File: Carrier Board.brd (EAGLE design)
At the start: 90 x 38.6 mm, 55 parts, among them J1 H4P-SMD-2.0, J2 H4P-SMD-2.0, J4 S2B-PH-SM4-TB(LF)(SN), J5 S2B-PH-SM4-TB(LF)(SN), Q1 MMBT2222A, SW2 MF-SW-TACT-6MM, U1 TMP36GRTZ, U2 TPL5010, U3 MB85RC64, U7 NAND

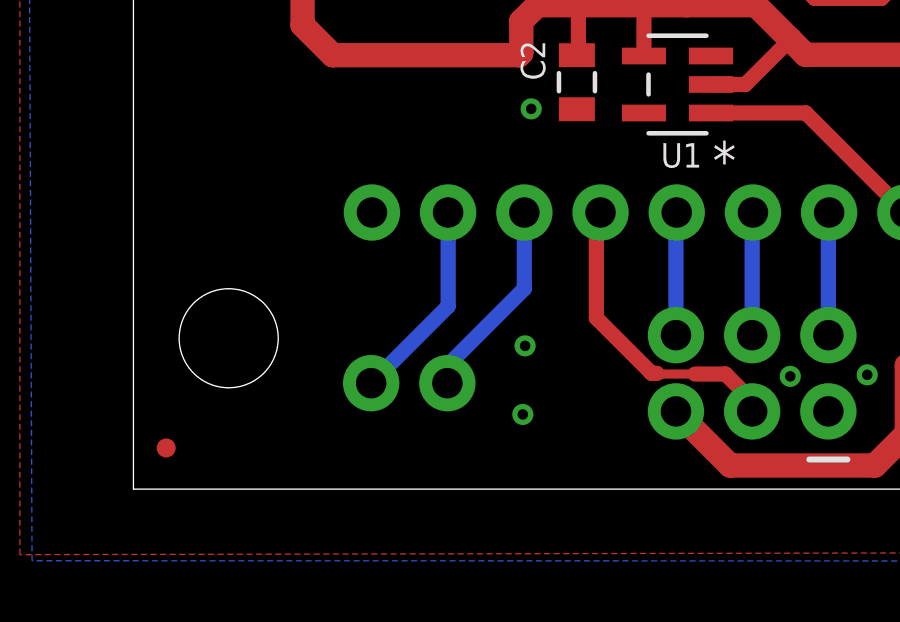
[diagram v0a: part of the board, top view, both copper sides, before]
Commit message: v1.1 - Added a GND pin to serial
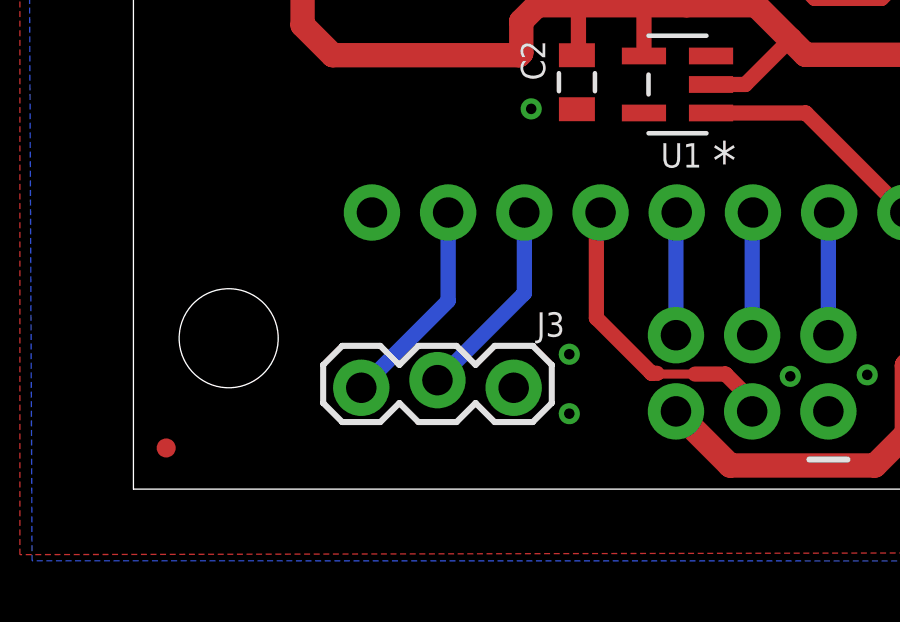
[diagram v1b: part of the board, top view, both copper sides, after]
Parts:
- J3: device SparkFun-Connectors:1X02 -> SparkFun-Connectors:1X03_LOCK
- moved J3 2.21 mm to (12.7, 3.51), flipped to the top, turned to 180 degrees
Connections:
- net GND: now also J3.1
- net RX: now also J3.2; no longer J3.1
- net TX: now also J3.3; no longer J3.2
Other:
- board text added: "GND Rx Tx"
- board text removed: "Rx Tx"

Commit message: Fixed Analoge Header Pins
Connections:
- net A0: now also J1.1; no longer J1.3
- net A1: now also J1.2; no longer J1.4
- net GND: now also J1.4; no longer J1.1
- net VCC-EXT: now also J1.3; no longer J1.2
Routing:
- net A0: track 12.8 -> 5.08 mm
- net A1: track 18.1 -> 13.0 mm
- net USER-SW: track 36.3 -> 39.1 mm
- net VCC-EXT: track 34.6 -> 36.0 mm, vias 1 -> 2
- net VCC2-EXT: vias 1 -> 2
- net SDA: vias 1 -> 2
- net SCL: vias 1 -> 2

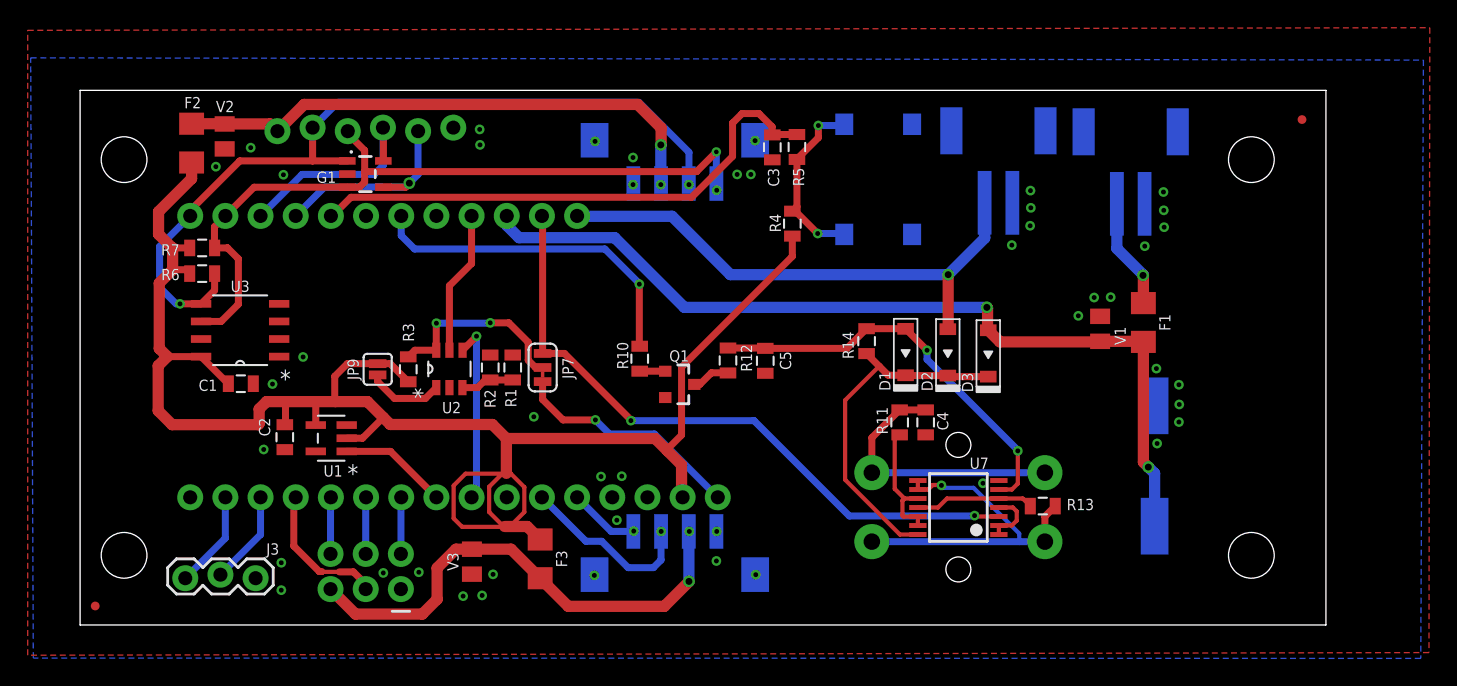
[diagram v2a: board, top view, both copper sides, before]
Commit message: Next major revision - Added RTC
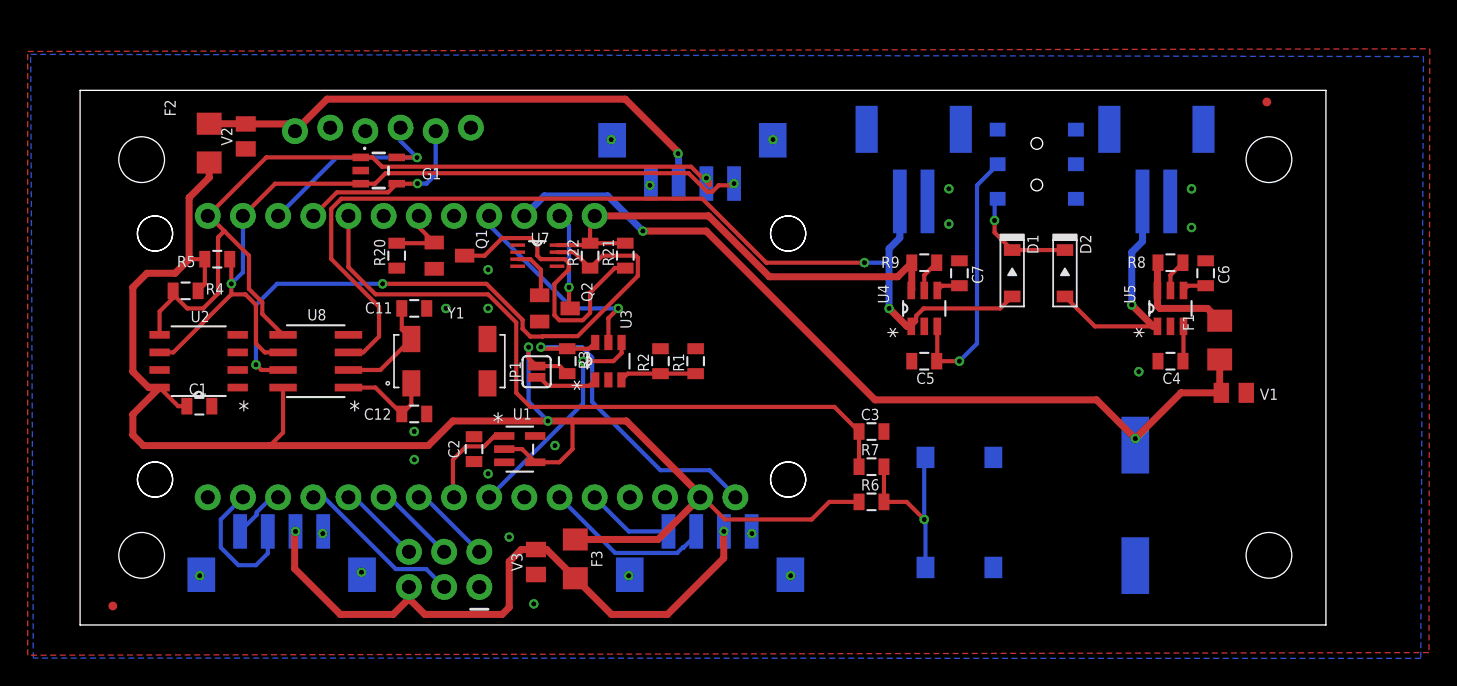
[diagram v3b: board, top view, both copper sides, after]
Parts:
- removed BORON/ARGON/XENON: PARTICLE-DEVICES-BORON, Carrier Board:PARTICLE-DEVICES_BORON
- removed D3: MF-DIO-SOD123-BAT42, MF_Discrete_Semiconductor:SOD-123
- removed JP7: JUMPER-SMT_3_1-NC_TRACE_SILK, SparkFun-Jumpers:SMT-JUMPER_3_1-NC_TRACE_SILK
- removed JP9: JUMPER-SMT_2_NC_PASTE_SILK, SparkFun-Jumpers:SMT-JUMPER_2_NC_PASTE_SILK
- removed R10: 10k, SparkFun-Passives:0805
- removed R11, R13, R14: 100k, SparkFun-Passives:0805
- removed R12: 100, SparkFun-Passives:0805
- removed S2: B3F-4000, adafruit:B3F-40XX-ROUND
- removed SW2: MF-SW-TACT-6MM, MF_Switches:TACT6MM
- added C11: 10pF, SparkFun-Capacitors:0805@1
- added C12: 8.2pF, SparkFun-Capacitors:0805@1
- added C6, C7: 0.1uF, SparkFun-Capacitors:0805@1
- added H1, H2, H3, H4: STAND-OFF-M2.5, Custom Components:STAND-OFF-M2.5
- added JP2: (no value), SparkFun-Connectors:1X06_LOCK
- added P1: PARTICLE-DEVICES-BORON, Carrier Board:PARTICLE-DEVICES_BORON
- added Q2: BSS138, transistor-small-signal:SOT23
- added R20, R21, R22: 10k, SparkFun-Passives:0805
- added R8, R9: 100, SparkFun-Passives:0805
- added S1: (no value), SparkFun-Switches:SWITCH_DPDT_SMD_AYZ0202
- added SW1: MF-SW-TACT-6MM, MF_Switches:TACT6MM
- added U4, U5: TPS22810, Custom Components:SOT-23-6
- added U8: MCP79410T-I/SN, Custom Components:SOIC8-N_MC
- added Y1: ECS-.327-6-17X-TR, Custom Components:XTAL_ECS-.327-6-17X-TR
- C4: value 0.1uF -> 10nF
- C5: value 1uF -> 10nF
- D1, D2: value MF-DIO-SOD123-BAT42 -> BAT42
- F1: value 1.5A - SLOW BLOW -> 6V/0.5A
- F2, F3: value 500mA - FAST BLOW -> 6V/0.5A
- J3: value (none) -> H4P-SMD-2.0; device SparkFun-Connectors:1X03_LOCK -> OPL_Connector:HW4-SMD-2.0
- J4: value S2B-PH-SM4-TB(LF)(SN) -> (none); device SparkFun-Connectors:JST-2-SMD -> SparkFun-Connectors:2X3
- J6: value (none) -> S2B-PH-SM4-TB(LF)(SN); device SparkFun-Connectors:2X3 -> SparkFun-Connectors:JST-2-SMD
- JP1: value (none) -> JUMPER-SMT_2_NC_PASTE_SILK; device SparkFun-Connectors:1X06_LOCK -> SparkFun-Jumpers:SMT-JUMPER_2_NC_PASTE_SILK
- JP3, JP4, JP5, JP6: device SparkFun:STAND-OFF -> SparkFun-Hardware:STAND-OFF
- Q1: value MMBT2222A -> BSS138; device SparkFun-DiscreteSemi:SOT23-3 -> transistor-small-signal:SOT23
- R4: value 100k -> 4.7k
- R5: value 10k -> 4.7k
- R6: value 4.7k -> 100k
- R7: value 4.7k -> 10k
- U2: value TPL5010 -> MB85RC64; device Custom Components:TSOT-23 -> Fujitsu_By_element14_Batch_1:SOIC127P600X175-8N
- U3: value MB85RC64 -> TPL5010; device Fujitsu_By_element14_Batch_1:SOIC127P600X175-8N -> Custom Components:TSOT-23
- U7: value NAND -> NL17SZ74USG; device adafruit:MC14093B-TSSOP14 -> Custom Components:SOP50P310X90-8N
- moved FRAME3 102.4 mm to (90.4, 19.3)
- moved J6 63.1 mm to (77.7, 34.3)
- moved J4 56.5 mm to (28.8, 2.74)
- moved R6 51.1 mm to (57.1, 8.89)
- moved R7 50.9 mm to (57.1, 11.4), turned to 0 degrees
- moved R4 44.1 mm to (7.62, 24.1), turned to 0 degrees
- moved R5 42.6 mm to (9.91, 26.4), turned to 180 degrees
- moved U7 35.4 mm to (33.0, 26.7), turned to 0 degrees
- moved U3 26.7 mm to (38.2, 19.1), turned to 90 degrees
- moved C3 21.7 mm to (57.1, 14.0), turned to 0 degrees
- moved Q1 19.0 mm to (26.7, 26.7)
- moved JP1 18.6 mm to (33.0, 18.3), flipped to the top, turned to 90 degrees
- moved C4 18.2 mm to (78.7, 19.1), turned to 180 degrees
- moved U2 18.1 mm to (8.56, 19.1), turned to 180 degrees
- moved C2 13.7 mm to (28.4, 12.7), turned to 90 degrees
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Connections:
- removed net !HARD-RESET: C5.1, D1.ANODE, R12.1, R14.1, U7.6
- removed net BUTTON-STATE: R13.1, U7.11, U7.5
- removed net DC-IN-EXT: F1.1, J4.2
- removed net ENABLE-PWR: D1.CATHODE, D2.CATHODE, D3.CATHODE, R14.2, U7.14
- removed net HARD-RESET: BORON/ARGON/XENON.D6, R10.2
- removed net N$1: U7.1, U7.2, U7.4
- removed net N$19: Q1.3, R12.2
- removed net N$24: C4.1, R11.2, S2.3, S2.4
- removed net N$25: R13.2, S2.1, S2.2, U7.8, U7.9
- removed net RESET: JP7.2, R3.1, U2.6
- new net BATT-IN: D1.ANODE, J5.2, U4.1, U8.3
- new net DEEP-SLEEP: P1.D6, Q1.1, R20.2
- new net EN/UVLO: C4.1, C5.1, S1.2, U4.3, U5.3
- new net N$10: C7.1, U4.4
- new net N$11: D2.ANODE, J6.2, U5.1
- new net N$12: R9.1, U4.5
- new net N$13: Q2.1, U7.3
- new net N$15: C12.1, U8.1, Y1.1
- new net N$2: P1.D5
- new net N$5: C6.1, U5.4
- new net N$6: R8.1, U5.5
- new net N$7: F1.1, R8.2, U5.6
- new net N$9: D1.CATHODE, D2.CATHODE, S1.3
- new net RTC-INT: R22.1, U7.7, U8.7
- net !RST: now also P1.RST, R3.1, U3.6; no longer BORON/ARGON/XENON.RST, JP7.3
- net A0: now also P1.A0; no longer BORON/ARGON/XENON.A0
- net A1: now also P1.A1; no longer BORON/ARGON/XENON.A1
- net A2: now also P1.A2; no longer BORON/ARGON/XENON.A2
- net D2: now also JP2.3, P1.D2; no longer BORON/ARGON/XENON.D2, JP1.3
- net D3: now also JP2.2, P1.D3; no longer BORON/ARGON/XENON.D3, JP1.2
- net DELAY: now also U3.3; no longer U2.3
- net DONE: now also P1.A3, U3.4; no longer BORON/ARGON/XENON.A3, U2.4
- net EN: now also P1.EN, Q2.3; no longer BORON/ARGON/XENON.EN, JP7.1, U7.3
- net GND: now also C11.2, C12.2, C6.2, C7.2, J3.4, J3.SS1, J3.SS2, JP2.1, P1.GND, Q2.2, R20.1, S1.1, SW1.P$3, SW1.P$4, U2.1, U2.3, U2.4, U2.7, U4.2, U5.2, U7.1, U7.2, U7.4, U8.4, Y1.2, Y1.3; no longer BORON/ARGON/XENON.GND, J3.1, JP1.1, SW2.P$3, SW2.P$4, U3.1, U3.3, U3.4, U3.7, U7.7
- net LI+: now also P1.LI+, R21.2, R22.2, R9.2, U4.6, U7.8; no longer BORON/ARGON/XENON.LI+, D2.ANODE, J5.2
- net MD: now also P1.MD; no longer BORON/ARGON/XENON.MD
- net MISO: now also J4.3, P1.MI; no longer BORON/ARGON/XENON.MI, J6.3
- net MOSI: now also J4.6, P1.MO; no longer BORON/ARGON/XENON.MO, J6.6
- net N$14: now also Q1.3, R21.1, U7.6; no longer R11.1, U7.10, U7.12, U7.13
- net N$16: now also C11.1, U8.2, Y1.4; no longer Q1.1, R10.1
- net N$4: now also R6.1, R7.2, SW1.P$1, SW1.P$2; no longer R4.1, R5.2, SW2.P$1, SW2.P$2
- net RX: now also J3.1, P1.RX; no longer BORON/ARGON/XENON.RX, J3.2
- net SCK: now also J4.4, P1.SCK; no longer BORON/ARGON/XENON.SCK, J6.4
- net SCL: now also JP2.4, P1.SCL, R5.1, U2.6, U8.6; no longer BORON/ARGON/XENON.SCL, JP1.4, R7.1, U3.6
- net SDA: now also JP2.5, P1.SDA, R4.1, U2.5, U8.5; no longer BORON/ARGON/XENON.SDA, JP1.5, R6.1, U3.5
- net SS: now also J4.2, P1.A5; no longer BORON/ARGON/XENON.A5, J6.2
- net TEMP: now also P1.A4; no longer BORON/ARGON/XENON.A4
- net TX: now also J3.2, P1.TX; no longer BORON/ARGON/XENON.TX, J3.3
- net USER-SW: now also P1.D4, R7.1; no longer BORON/ARGON/XENON.D4, R5.1
- net VCC: now also JP1.2, P1.3V3, R5.2, U2.8, U8.8; no longer BORON/ARGON/XENON.3V3, JP9.2, R7.2, U3.8
- net VCC-EXT: now also J3.3, J4.5; no longer J6.5
- net VCC2-EXT: now also JP2.6; no longer JP1.6
- net VDD: now also JP1.1, U3.1; no longer JP9.1, U2.1
- net VUSB: now also P1.VUSB; no longer BORON/ARGON/XENON.VUSB, D3.ANODE
- net WAKE: now also P1.D8, U3.5; no longer BORON/ARGON/XENON.D8, U2.5
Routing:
- net BATT-IN: track 0.00 -> 74.5 mm, vias 0 -> 2
- net RTC-INT: track 0.00 -> 46.5 mm, vias 0 -> 2
- net EN: track 47.9 -> 7.00 mm, vias 2 -> 1
- net !HARD-RESET: track 29.5 -> 0.00 mm, vias 2 -> 0
- net ENABLE-PWR: track 25.6 -> 0.00 mm
- net N$25: track 25.5 -> 0.00 mm, vias 1 -> 0
- net HARD-RESET: track 24.6 -> 0.00 mm, vias 1 -> 0
- net EN/UVLO: track 0.00 -> 22.0 mm, vias 0 -> 1
- net N$24: track 19.7 -> 0.00 mm
- net N$11: track 0.00 -> 17.9 mm, vias 0 -> 1
- net RESET: track 14.0 -> 0.00 mm, vias 2 -> 0
- net N$14: track 9.10 -> 21.1 mm
- net USER-SW: track 39.1 -> 51.0 mm
- net VCC: track 131.9 -> 121.1 mm, vias 0 -> 2
- net VCC-EXT: track 36.0 -> 46.5 mm
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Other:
- board text added: "DC - IN"
- board text added: "GND Vcc A1 A0"
- board text added: "GND Vcc Rx Tx"
- board text added: "SS SCK MOSI"
- board text removed: "5-6V @ 10W"
- board text removed: "A1 A0 Vcc GND"
- board text removed: "GND Rx Tx"
- board text removed: "MOSI SCK SS"

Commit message: Added Zener protection for Argon / Xenon
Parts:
- added D3: 6.2V/500mW, SparkFun-DiscreteSemi:PANASONIC_SMINI2-F5-B
- added JP7: JUMPER-SMT_2_NC_PASTE_SILK, SparkFun-Jumpers:SMT-JUMPER_2_NC_PASTE_SILK
- moved R21 9.40 mm to (30.0, 26.7), turned to 270 degrees
- moved Q2 3.82 mm to (34.0, 26.7)
- moved U7 3.78 mm to (34.3, 23.1), turned to 180 degrees
- moved R22 0.51 mm to (37.3, 26.7)
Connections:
- removed net N$11: D2.ANODE, J6.2, U5.1
- new net DC-IN: D2.ANODE, J6.2, JP7.1, U5.1
- new net N$1: D3.C, JP7.2
- net GND: now also D3.A
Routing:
- net EN/UVLO: track 22.0 -> 40.4 mm
- net N$11: track 17.9 -> 0.00 mm, vias 1 -> 0
- net DC-IN: track 0.00 -> 17.8 mm, vias 0 -> 3
- net SCL: track 59.5 -> 71.0 mm
- net N$14: track 21.1 -> 10.4 mm
- net LI+: track 34.3 -> 43.5 mm, vias 0 -> 1
- net RTC-INT: track 46.5 -> 38.6 mm
- net N$1: track 0.00 -> 5.66 mm, vias 0 -> 1
- net EN: track 7.00 -> 3.08 mm, vias 1 -> 0
- net VCC: track 121.1 -> 123.5 mm
- net WAKE: track 15.2 -> 17.3 mm
- net N$13: track 3.87 -> 5.94 mm
- net BATT-IN: track 74.5 -> 75.6 mm, vias 2 -> 4
- net SDA: track 63.4 -> 64.5 mm
- net D2: track 15.9 -> 16.5 mm
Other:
- board text added: "ON"
- board text added: "Over Voltage Protection Must be connected for Argon / Xenon. Optional for Boron"
- board text added: "Power Switch"
- board text removed: "Power - Push On / Push Off"

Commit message: Final Tweaks before MacroFab
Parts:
- F1: value 6V/0.5A -> 63V/1.5A
- J2: value H4P-SMD-2.0 -> (none); device OPL_Connector:HW4-SMD-2.0 -> SparkFun-Connectors:2X3
- J4: value (none) -> S2B-PH-SM4-TB(LF)(SN); device SparkFun-Connectors:2X3 -> SparkFun-Connectors:JST-2-SMD
- J6: value S2B-PH-SM4-TB(LF)(SN) -> H4P-SMD-2.0; device SparkFun-Connectors:JST-2-SMD -> OPL_Connector:HW4-SMD-2.0
- moved J4 58.2 mm to (77.7, 34.3)
- moved J6 33.6 mm to (44.2, 31.9)
- moved J2 33.0 mm to (28.8, 2.74)
- moved C1 0.51 mm to (8.61, 15.3)
- renumbered JP2 to J7
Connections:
- net DC-IN: now also J4.2; no longer J6.2
- net GND: now also J2.1, J6.4, J6.SS1, J6.SS2; no longer J2.4, J2.SS1, J2.SS2, J6.1
- net MISO: now also J2.3; no longer J4.3
- net MOSI: now also J2.6; no longer J4.6
- net SCK: now also J2.4; no longer J4.4
- net SCL: now also J6.1; no longer J2.1
- net SDA: now also J6.2; no longer J2.2
- net SS: now also J2.2; no longer J4.2
- net VCC-EXT: now also J2.5; no longer J4.5
- net VCC2-EXT: now also J6.3; no longer J2.3
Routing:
- net DC-IN: track 17.8 -> 20.6 mm
- net BATT-IN: track 75.6 -> 77.3 mm
- net VCC: track 123.5 -> 124.9 mm
- net A0: track 6.35 -> 6.82 mm, vias 0 -> 1
- net RX: track 3.87 -> 4.03 mm, vias 0 -> 1
- net VCC2-EXT: track 38.9 -> 39.1 mm, vias 1 -> 2
- net TX: track 10.2 -> 10.3 mm, vias 0 -> 1
- net A1: track 12.4 -> 12.3 mm, vias 0 -> 1
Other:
- board text added: "v1.1- 10-29-19"
- board text removed: "v1.1- 9-18-19"
